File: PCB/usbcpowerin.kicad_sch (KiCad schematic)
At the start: 34 parts, among them CN1002 Conn_ARM_JTAG_SWD_10, J1001 USB_C_Receptacle, U1001 SPX3819M5-L-3-3, U1002 STM32F030F4Px, U1003 FUSB302BMPX, U1004 USBLC6-2SC6

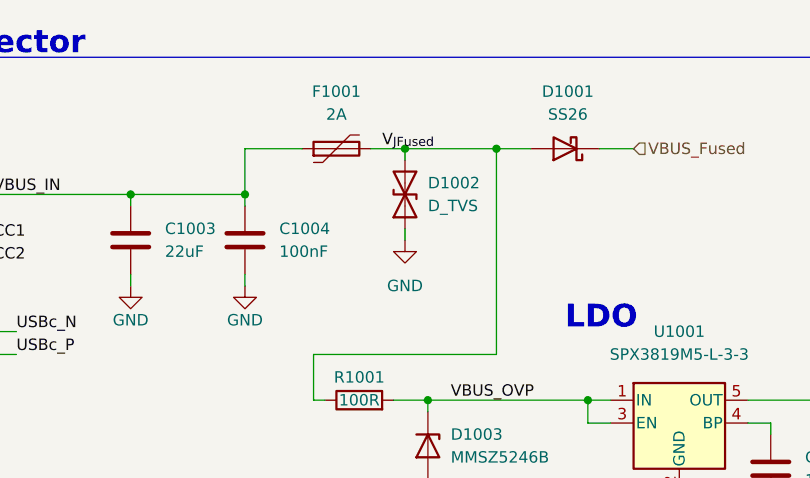
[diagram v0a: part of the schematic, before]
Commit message: Modified schematic
changed C1003 size to 1206
flipped D1002 around
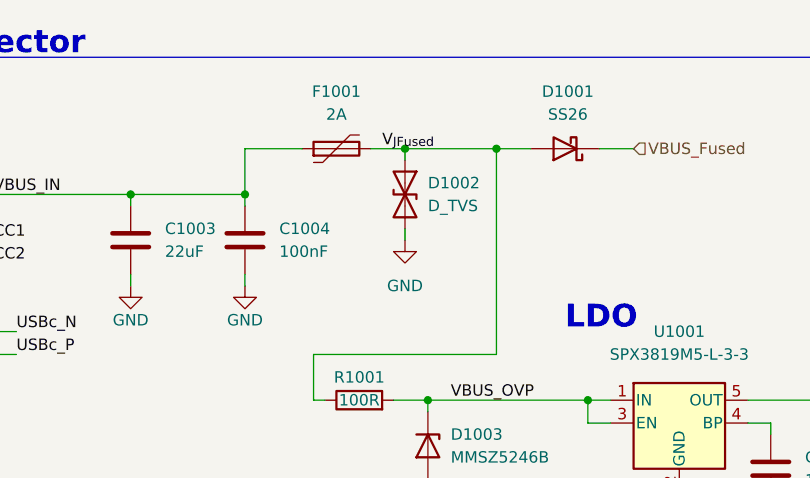
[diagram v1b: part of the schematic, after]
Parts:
- C1003: footprint Capacitor_SMD:C_0603_1608Metric -> Capacitor_SMD:C_1206_3216Metric
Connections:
- net GND: now also D1002.2 (A2); no longer D1002.1 (A1)
- net V_{JFused}: now also D1002.1 (A1); no longer D1002.2 (A2)
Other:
- moved on the sheet: D1002
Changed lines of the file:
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@@
       (effects (font (size 1.27 1.27)) (justify left))
     )
-    (property "Footprint" "Capacitor_SMD:C_0603_1608Metric" (id 2) (at 69.5452 49.53 0)
+    (property "Footprint" "Capacitor_SMD:C_1206_3216Metric" (id 2) (at 69.5452 49.53 0)
       (effects (font (size 1.27 1.27)) hide)
     )
@@
     (pin "2")
   )
-  (symbol (lib_id "Device:D_TVS") (at 99.06 40.64 90) (unit 1)
+  (symbol (lib_id "Device:D_TVS") (at 99.06 40.64 270) (unit 1)
     (in_bom yes) (on_board yes) (fields_autoplaced)
     (property "Reference" "D1002" (id 0) (at 101.6 39.3699 90)
-      (effects (font (size 1.27 1.27)) (justify right))
+      (effects (font (size 1.27 1.27)) (justify left))
     )
     (property "Value" "D_TVS" (id 1) (at 101.6 41.9099 90)
-      (effects (font (size 1.27 1.27)) (justify right))
+      (effects (font (size 1.27 1.27)) (justify left))
     )
     (property "Footprint" "Diode_SMD:D_SMA" (id 2) (at 99.06 40.64 0)
